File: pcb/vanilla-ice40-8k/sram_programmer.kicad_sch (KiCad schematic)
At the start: 33 parts, among them U2 W25X40CLSN, U3 FT2232HQ, U4 93LCxxBxxOT, Y1 12Mhz/18pf

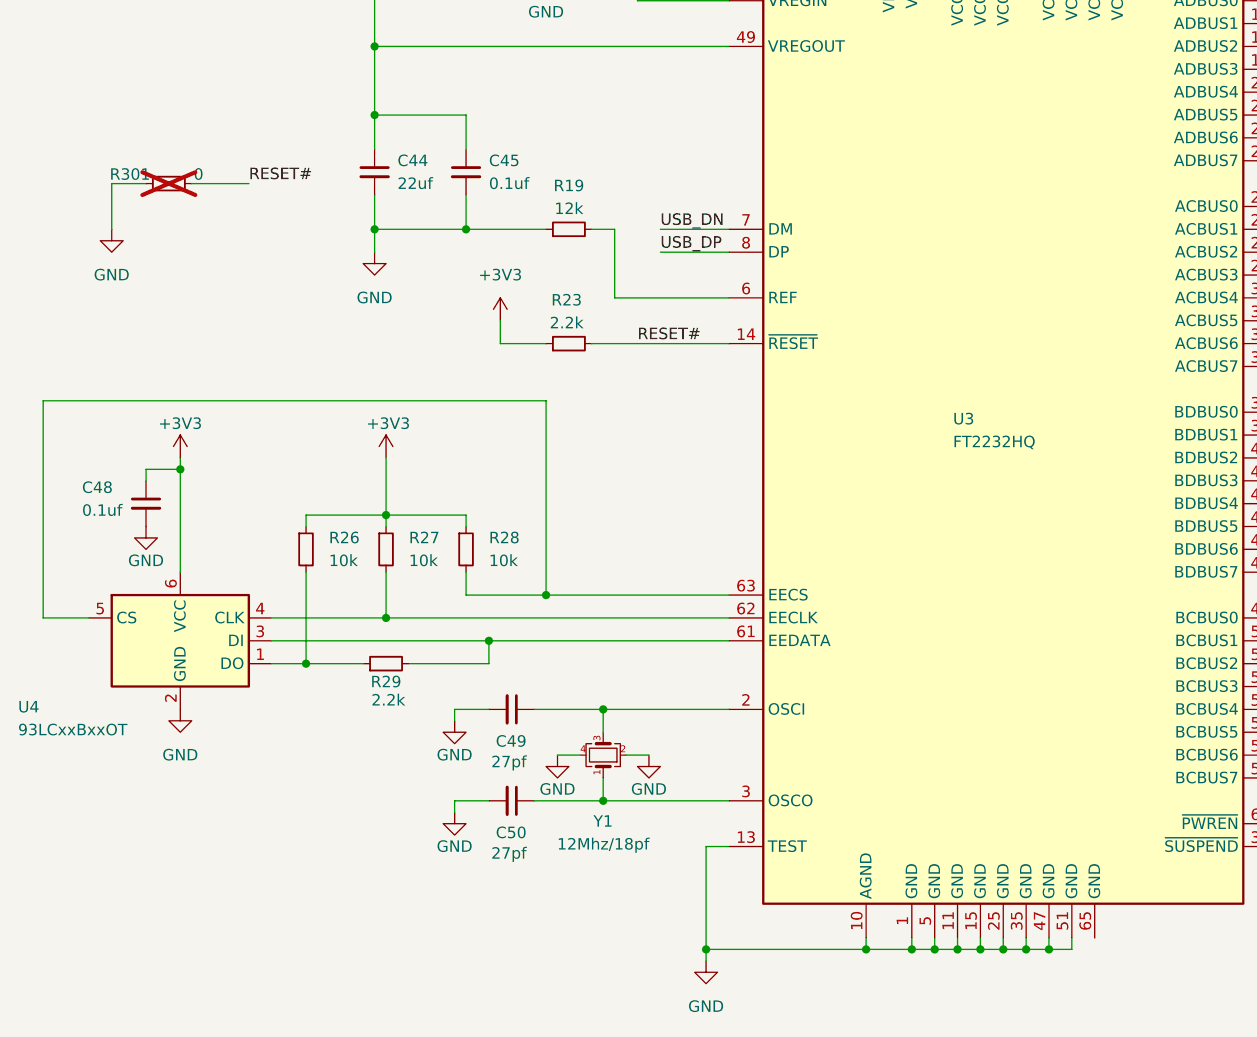
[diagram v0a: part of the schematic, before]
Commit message: [hx8k][pcb] rough layout of full board
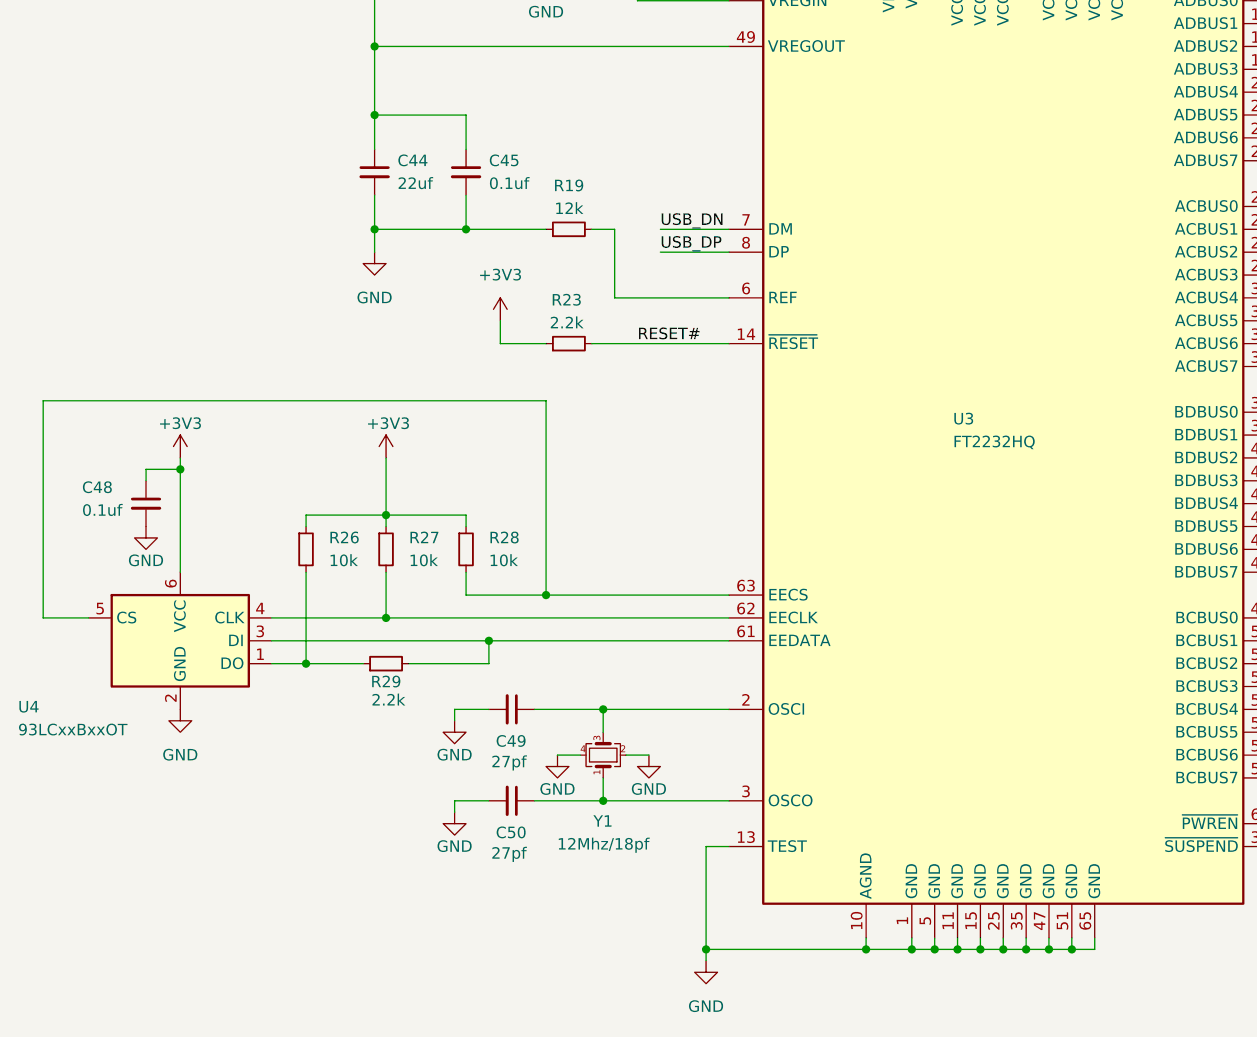
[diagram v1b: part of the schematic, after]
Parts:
- removed R301: 0, Resistor_SMD:R_0603_1608Metric, symbol Device:R_Small
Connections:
- net GND: now also U3.65 (GND)
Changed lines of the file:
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@@
 	)
 	(junction
+		(at 152.4 207.01)
+		(diameter 0)
+		(color 0 0 0 0)
+	)
+	(junction
 		(at 153.67 78.74)
 		(diameter 0)
@@
 	(wire
 		(pts
-			(xy 49.53 121.92) (xy 45.72 121.92)
-		)
-		(stroke
-			(width 0)
-			(type default)
-		)
-	)
-	(wire
-		(pts
 			(xy 104.14 101.6) (xy 114.3 101.6)
 		)
@@
 	(wire
 		(pts
-			(xy 45.72 121.92) (xy 45.72 127)
-		)
-		(stroke
-			(width 0)
-			(type default)
-		)
-	)
-	(wire
-		(pts
 			(xy 144.78 86.36) (xy 144.78 91.44)
 		)
@@
 	(wire
 		(pts
+			(xy 154.94 207.01) (xy 152.4 207.01)
+		)
+		(stroke
+			(width 0)
+			(type default)
+		)
+	)
+	(wire
+		(pts
 			(xy 369.57 137.16) (xy 354.33 137.16)
 		)
@@
 	(wire
 		(pts
-			(xy 54.61 121.92) (xy 60.96 121.92)
-		)
-		(stroke
-			(width 0)
-			(type default)
-		)
-	)
-	(wire
-		(pts
 			(xy 74.93 106.68) (xy 114.3 106.68)
 		)
@@
 	(wire
 		(pts
+			(xy 154.94 205.74) (xy 154.94 207.01)
+		)
+		(stroke
+			(width 0)
+			(type default)
+		)
+	)
+	(wire
+		(pts
 			(xy 53.34 152.4) (xy 53.34 153.67)
 		)
@@
 	)
 	(label "RESET#"
-		(at 60.96 121.92 0)
-		(effects
-			(font
-				(size 1.27 1.27)
-			)
-			(justify left bottom)
-		)
-	)
-	(label "RESET#"
 		(at 104.14 139.7 0)
 		(effects
@@
 	(symbol
 		(lib_id "power:GND")
-		(at 45.72 127 0)
-		(unit 1)
-		(exclude_from_sim no)
-		(in_bom yes)
-		(on_board yes)
-		(dnp no)
-		(fields_autoplaced yes)
-		(property "Reference" "#PWR052"
-			(at 45.72 133.35 0)
-			(effects
-				(font
-					(size 1.27 1.27)
-				)
-				(hide yes)
-			)
-		)
-		(property "Value" "GND"
-			(at 45.72 132.08 0)
-			(effects
-				(font
-					(size 1.27 1.27)
-				)
-			)
-		)
-		(property "Footprint" ""
-			(at 45.72 127 0)
-			(effects
-				(font
-					(size 1.27 1.27)
-				)
-				(hide yes)
-			)
-		)
-		(property "Datasheet" ""
-			(at 45.72 127 0)
-			(effects
-				(font
-					(size 1.27 1.27)
-				)
-				(hide yes)
-			)
-		)
-		(property "Description" "Power symbol creates a global label with name \"GND\" , ground"
-			(at 45.72 127 0)
-			(effects
-				(font
-					(size 1.27 1.27)
-				)
-				(hide yes)
-			)
-		)
-		(pin "1"
-		)
-		(instances
-			(project "vanilla-ice40-8k"
-				(path "/6fdfbf4b-014a-4077-8dc3-7ce5ecaf5fe5/8fcffd86-9b82-4947-9420-a56f34009c5e"
-					(reference "#PWR052")
-					(unit 1)
-				)
-			)
-		)
-	)
-	(symbol
-		(lib_id "power:GND")
 		(at 83.82 191.77 0)
 		(unit 1)
@@
 					(unit 1)
 				)
-			)
-		)
-	)
-	(symbol
-		(lib_id "Device:R_Small")
-		(at 52.07 121.92 90)
-		(unit 1)
-		(exclude_from_sim no)
-		(in_bom no)
-		(on_board yes)
-		(dnp yes)
-		(property "Reference" "R301"
-			(at 47.752 120.904 90)
-			(effects
-				(font
-					(size 1.27 1.27)
-				)
-			)
-		)
-		(property "Value" "0"
-			(at 55.372 120.904 90)
-			(effects
-				(font
-					(size 1.27 1.27)
-				)
-			)
-		)
-		(property "Footprint" "Resistor_SMD:R_0603_1608Metric"
-			(at 52.07 121.92 0)
-			(effects
-				(font
-					(size 1.27 1.27)
-				)
-				(hide yes)
-			)
-		)
-		(property "Datasheet" "~"
-			(at 52.07 121.92 0)
-			(effects
-				(font
-					(size 1.27 1.27)
-				)
-				(hide yes)
-			)
-		)
-		(property "Description" "Resistor, small symbol"
-			(at 52.07 121.92 0)
-			(effects
-				(font
-					(size 1.27 1.27)
-				)
-				(hide yes)
-			)
-		)
-		(property "LCSC Part #" "C21189"
-			(at 52.07 121.92 0)
-			(effects
-				(font
-					(size 1.27 1.27)
-				)
-				(hide yes)
-			)
-		)
-		(property "JLCPCB Rotation Offset" ""
-			(at 52.07 121.92 0)
-			(effects
-				(font
-					(size 1.27 1.27)
-				)
-				(hide yes)
-			)
-		)
-		(property "Digi-Key Part Number" "CR0603-J/-000ELFCT-ND"
-			(at 52.07 121.92 0)
-			(effects
-				(font
-					(size 1.27 1.27)
-				)
-				(hide yes)
-			)
-		)
-		(pin "2"
-		)
-		(pin "1"
-		)
-		(instances
-			(project "vanilla-ice40-8k"
-				(path "/6fdfbf4b-014a-4077-8dc3-7ce5ecaf5fe5/8fcffd86-9b82-4947-9420-a56f34009c5e"
-					(reference "R301")
-					(unit 1)
-				)

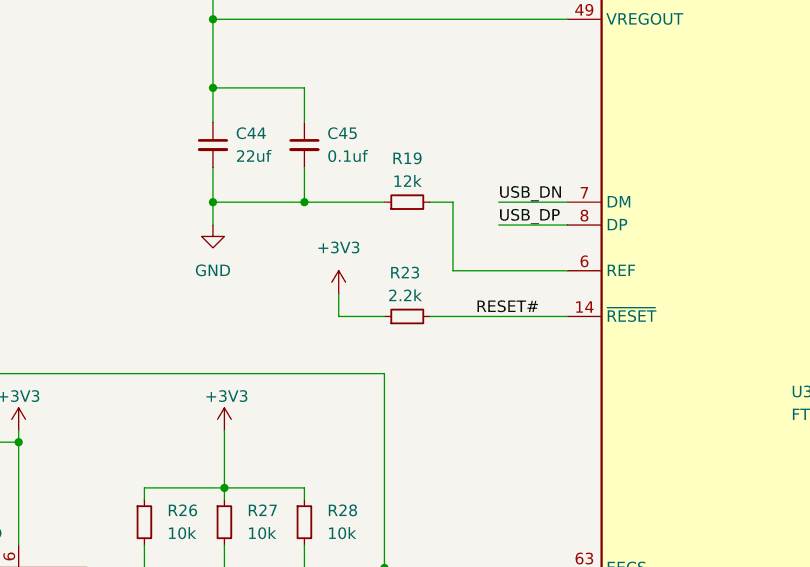
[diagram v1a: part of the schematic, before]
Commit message: [hx8k][pcb] rough layout improvements
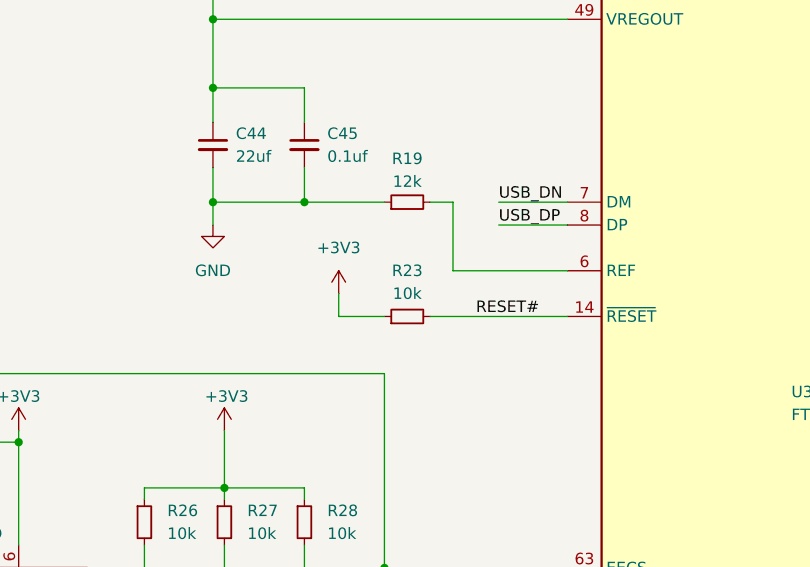
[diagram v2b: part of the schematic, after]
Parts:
- R23: value 2.2k -> 10k; Digi-Key Part Number 118-CR0603-FX-2201ELFCT-ND -> CR0603-FX-1002ELFCT-ND; LCSC Part # C4190 -> C25804
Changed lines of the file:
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@@
+	(symbol
+		(lib_id "Device:R_Small")
+		(at 96.52 139.7 90)
+		(unit 1)
+		(exclude_from_sim no)
+		(in_bom yes)
+		(on_board yes)
+		(dnp no)
+		(fields_autoplaced yes)
+		(property "Reference" "R23"
+			(at 96.52 134.62 90)
+			(effects
+				(font
+					(size 1.27 1.27)
+				)
+			)
+		)
+		(property "Value" "10k"
+			(at 96.52 137.16 90)
+			(effects
+				(font
+					(size 1.27 1.27)
+				)
+			)
+		)
+		(property "Footprint" "Resistor_SMD:R_0603_1608Metric"
+			(at 96.52 139.7 0)
+			(effects
+				(font
+					(size 1.27 1.27)
+				)
+				(hide yes)
+			)
+		)
+		(property "Datasheet" "~"
+			(at 96.52 139.7 0)
+			(effects
+				(font
+					(size 1.27 1.27)
+				)
+				(hide yes)
+			)
+		)
+		(property "Description" "Resistor, small symbol"
+			(at 96.52 139.7 0)
+			(effects
+				(font
+					(size 1.27 1.27)
+				)
+				(hide yes)
+			)
+		)
+		(property "LCSC Part #" "C25804"
+			(at 96.52 139.7 0)
+			(effects
+				(font
+					(size 1.27 1.27)
+				)
+				(hide yes)
+			)
+		)
+		(property "JLCPCB Rotation Offset" ""
+			(at 96.52 139.7 0)
+			(effects
+				(font
+					(size 1.27 1.27)
+				)
+				(hide yes)
+			)
+		)
+		(property "Digi-Key Part Number" "CR0603-FX-1002ELFCT-ND"
+			(at 96.52 139.7 0)
+			(effects
+				(font
+					(size 1.27 1.27)
+				)
+				(hide yes)
+			)
+		)
+		(pin "2"
+		)
+		(pin "1"
+		)
+		(instances
+			(project "vanilla-ice40-8k"
+				(path "/6fdfbf4b-014a-4077-8dc3-7ce5ecaf5fe5/8fcffd86-9b82-4947-9420-a56f34009c5e"
+					(reference "R23")
+					(unit 1)
+				)
+			)
+		)
+	)
 	(symbol
 		(lib_id "Device:R_Small")
@@
 					(unit 1)
 				)
-			)
-		)
-	)
-	(symbol
-		(lib_id "Device:R_Small")
-		(at 96.52 139.7 90)
-		(unit 1)
-		(exclude_from_sim no)
-		(in_bom yes)
-		(on_board yes)
-		(dnp no)
-		(property "Reference" "R23"
-			(at 96.266 134.874 90)
-			(effects
-				(font
-					(size 1.27 1.27)
-				)
-			)
-		)
-		(property "Value" "2.2k"
-			(at 96.266 137.414 90)
-			(effects
-				(font
-					(size 1.27 1.27)
-				)
-			)
-		)
-		(property "Footprint" "Resistor_SMD:R_0603_1608Metric"
-			(at 96.52 139.7 0)
-			(effects
-				(font
-					(size 1.27 1.27)
-				)
-				(hide yes)
-			)
-		)
-		(property "Datasheet" "~"
-			(at 96.52 139.7 0)
-			(effects
-				(font
-					(size 1.27 1.27)
-				)
-				(hide yes)
-			)
-		)
-		(property "Description" "Resistor, small symbol"
-			(at 96.52 139.7 0)
-			(effects
-				(font
-					(size 1.27 1.27)
-				)
-				(hide yes)
-			)
-		)
-		(property "LCSC Part #" "C4190"
-			(at 96.52 139.7 0)
-			(effects
-				(font
-					(size 1.27 1.27)
-				)
-				(hide yes)
-			)
-		)
-		(property "JLCPCB Rotation Offset" ""
-			(at 96.52 139.7 0)
-			(effects
-				(font
-					(size 1.27 1.27)
-				)
-				(hide yes)
-			)
-		)
-		(property "Digi-Key Part Number" "118-CR0603-FX-2201ELFCT-ND"
-			(at 96.52 139.7 0)
-			(effects
-				(font
-					(size 1.27 1.27)
-				)
-				(hide yes)
-			)
-		)
-		(pin "2"
-		)
-		(pin "1"
-		)
-		(instances
-			(project "vanilla-ice40-8k"
-				(path "/6fdfbf4b-014a-4077-8dc3-7ce5ecaf5fe5/8fcffd86-9b82-4947-9420-a56f34009c5e"
-					(reference "R23")
-					(unit 1)
-				)

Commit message: [hx8k][pcb] move top level to use symbol lib
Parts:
- C36, C38, C39, C40, C41, C42, C43, C45, C46, C48: symbol Device:C_Small -> !Misc:C_0.1uf_0402
- R18, R20, R21, R22, R23, R26, R27, R28: symbol Device:R_Small -> !Misc:R_10K_0603
- R19, R29: symbol Device:R_Small -> !Misc:R_2.2K_0603

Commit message: [hx8k][pcb] move usb_c_power to use symbol lib
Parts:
- C35, C37, C44, C47: symbol Device:C_Small -> !Misc:C_22uf_0603; LCSC Part # C59461 -> C59461
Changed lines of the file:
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@@
 	)
 	(symbol
-		(lib_id "Device:C_Small")
+		(lib_id "!Misc:C_22uf_0603")
 		(at 74.93 120.65 0)
 		(unit 1)
@@
 			)
 		)
-		(property "Description" "Unpolarized capacitor, small symbol"
+		(property "Description" "Unpolarized capacitor 22uf 0603 6.3V"
 			(at 74.93 120.65 0)
 			(effects
@@
 			)
 		)
-		(property "LCSC Part #" "C59461"
+		(property "LCSC Part #" " C59461"
 			(at 74.93 120.65 0)
 			(effects
@@
 	)
 	(symbol
-		(lib_id "Device:C_Small")
+		(lib_id "!Misc:C_22uf_0603")
 		(at 110.49 81.28 0)
 		(unit 1)
@@
 			)
 		)
-		(property "Description" "Unpolarized capacitor, small symbol"
+		(property "Description" "Unpolarized capacitor 22uf 0603 6.3V"
 			(at 110.49 81.28 0)
 			(effects
@@
 			)
 		)
-		(property "LCSC Part #" "C59461"
+		(property "LCSC Part #" " C59461"
 			(at 110.49 81.28 0)
 			(effects
@@
 	)
 	(symbol
-		(lib_id "Device:C_Small")
+		(lib_id "!Misc:C_22uf_0603")
 		(at 110.49 63.5 0)
 		(unit 1)
@@
 			)
 		)
-		(property "Description" "Unpolarized capacitor, small symbol"
+		(property "Description" "Unpolarized capacitor 22uf 0603 6.3V"
 			(at 110.49 63.5 0)
 			(effects
@@
 			)
 		)
-		(property "LCSC Part #" "C59461"
+		(property "LCSC Part #" " C59461"
 			(at 110.49 63.5 0)
 			(effects
@@
 	)
 	(symbol
-		(lib_id "Device:C_Small")
+		(lib_id "!Misc:C_22uf_0603")
 		(at 288.29 124.46 0)
 		(unit 1)
@@
 			)
 		)
-		(property "Description" "Unpolarized capacitor, small symbol"
+		(property "Description" "Unpolarized capacitor 22uf 0603 6.3V"
 			(at 288.29 124.46 0)
 			(effects
@@
 			)
 		)
-		(property "LCSC Part #" "C59461"
+		(property "LCSC Part #" " C59461"
 			(at 288.29 124.46 0)
 			(effects
